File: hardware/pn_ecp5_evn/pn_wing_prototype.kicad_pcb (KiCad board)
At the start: 4 copper layers, 129.5 x 52.2 mm, 257 parts, among them J101 Screw_Terminal_01x02, J102 Conn_Coaxial, J103 Conn_02x20_Odd_Even, J104 Conn_Coaxial, J105 Conn_Coaxial, J106 Conn_Coaxial, J107 Conn_01x10, J201 Conn_Coaxial, J301 Conn_Coaxial, J401 Conn_Coaxial, J601 Conn_Coaxial, J701 Conn_Coaxial, J702 Conn_Coaxial, J703 Conn_Coaxial, U201 VEMI65AB-HCI, U202 LMX2594, U301 PAT1220-C-3DB, U302 TRF37A73, U303 PAT1220-C-3DB, U401 PAT1220-C-3DB, U402 TRF37A73, U403 PAT1220-C-3DB, U501 LM27761, U502 ADM7171ACPZ-3.3-R7, U503 TPS72301DB, U601 LM2904, U602 OPA2211, U701 SYM-63LH+, U702 ADG621, U703 OPA2211, U801 THS4551, U802 LT6657BHMS8-2.5, U901 ADS7868, U902 ADS7868, U903 Si8640BB-B-IU, U904 Si8640BB-B-IU, U905 Si8642BB-B-IU, X601 ABLNO

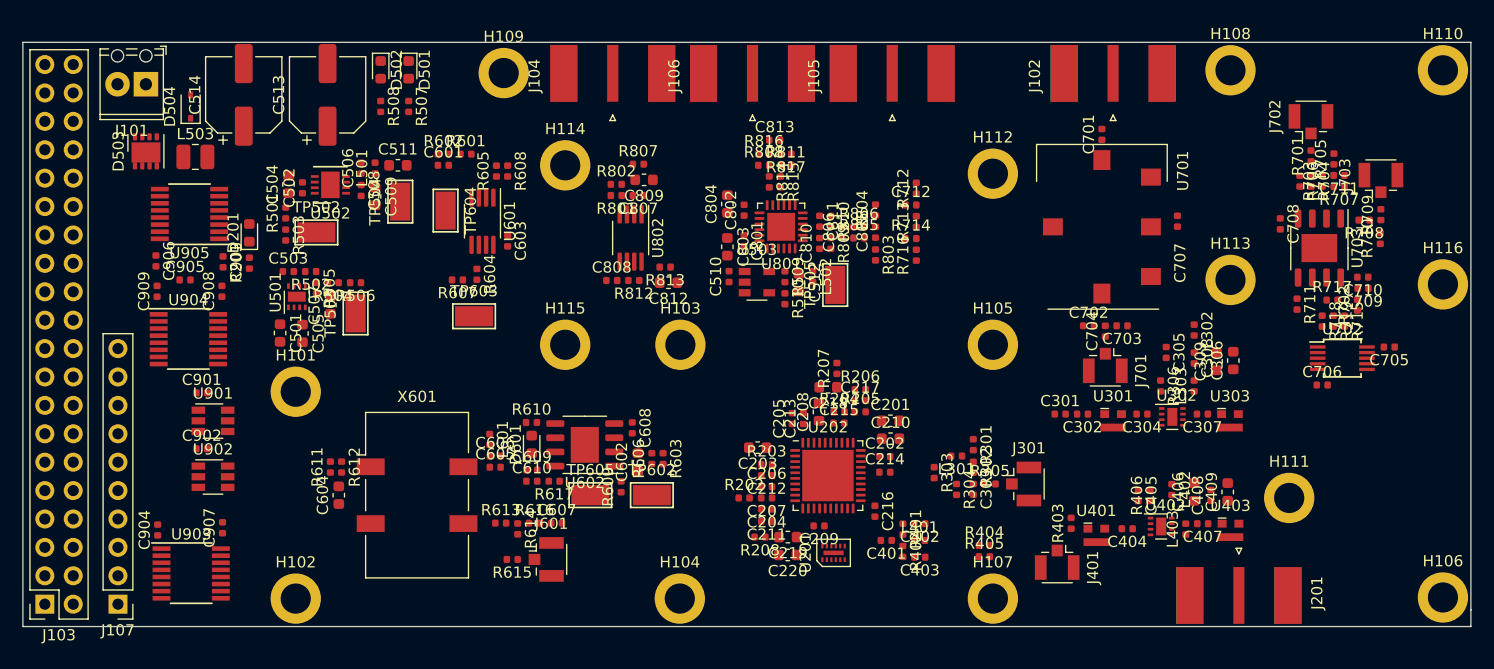
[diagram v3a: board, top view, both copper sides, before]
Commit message: work on routing phase noise downconverter
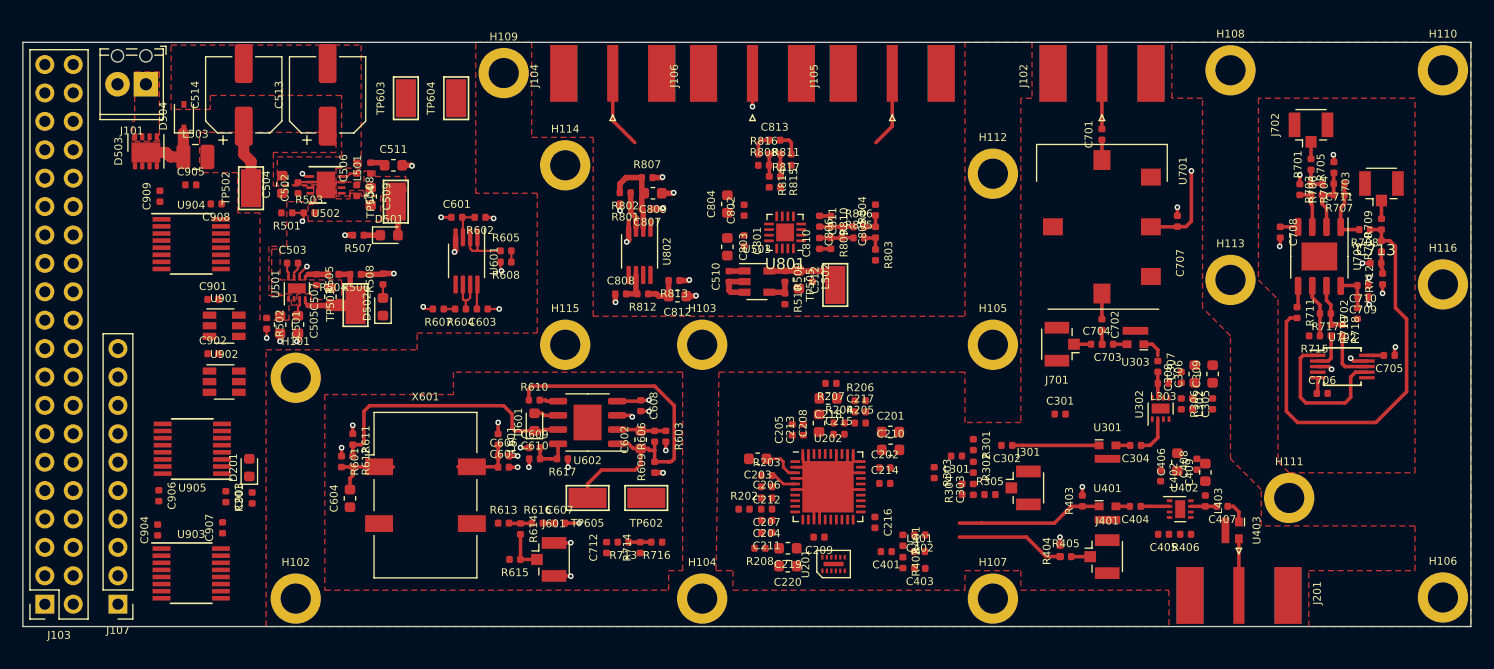
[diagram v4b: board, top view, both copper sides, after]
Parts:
- added C713: DNI, Capacitor_SMD:C_0402_1005Metric, F.Cu at (151.0, 85.5)
- U801: footprint Package_CSP:LFCSP-24-1EP_4x4mm_P0.5mm_EP2.5x2.5mm -> Package_DFN_QFN:VQFN-16-1EP_3x3mm_P0.5mm_EP1.6x1.6mm
- moved R712 42.5 mm to (151.6, 86.9)
- moved C712 41.0 mm to (82.2, 110.9), turned to 90 degrees
- moved R713 38.8 mm to (83.7, 110.5), turned to 180 degrees
- moved R714 36.7 mm to (85.2, 110.9), turned to 90 degrees
- moved R716 34.6 mm to (86.7, 110.5), turned to 180 degrees
- moved R601 29.7 mm to (58.5, 103.2), turned to 270 degrees
- moved D502 21.2 mm to (62.2, 89.4), turned to 90 degrees
- moved C903 21.0 mm to (48.1, 106.4)
- moved C906 21.0 mm to (42.1, 106.3)
- moved R201 21.0 mm to (50.5, 106.5)
- moved U905 21.0 mm to (45.1, 102.1)
- moved D201 21.0 mm to (50.2, 103.8)
- moved TP603 20.4 mm to (64.2, 70.8), turned to 90 degrees
- moved R508 15.4 mm to (62.2, 86.9), turned to 90 degrees
- moved D501 14.9 mm to (62.8, 83.0), turned to 0 degrees
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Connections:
- J103 pad 31: /isolator/BUF_~PD~_ISO -> /isolator/BUF_~PD
- U903 pad 13: /IF_G2 -> /LMX_CSB
- U903 pad 14: /IF_G1 -> /LMX_SDI
- U903 pad 3: /isolator/IF_G1 -> /isolator/LMX_SDI
- U903 pad 4: /isolator/IF_G2 -> /isolator/LMX_CS
- U904 pad 13: /LMX_SDI -> /IF_G2
- U904 pad 14: /LMX_CSB -> /IF_G1
- U904 pad 3: /isolator/LMX_CS -> /isolator/IF_G1
- U904 pad 4: /isolator/LMX_SDI -> /isolator/IF_G2
- U905 pad 11: /BUF_~PD -> /isolator/BUF_~PD
- U905 pad 6: /isolator/BUF_~PD~_ISO -> /BUF_~PD
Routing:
- net GND: track 0.00 -> 76.4 mm, vias 0 -> 37
- net Net-(R708-Pad1): track 0.00 -> 38.3 mm
- net Net-(C602-Pad1): track 0.00 -> 35.2 mm
- net Net-(D601-Pad1): track 0.00 -> 24.1 mm
- net Net-(R715-Pad1): track 0.00 -> 18.3 mm
- net Net-(C402-Pad1): track 0.00 -> 13.1 mm
- net -3V3: track 0.00 -> 12.8 mm, vias 0 -> 2
- net Net-(C707-Pad2): track 0.00 -> 10.6 mm, vias 0 -> 1
- net Net-(C403-Pad1): track 0.00 -> 9.72 mm
- net /adc/VOUT_P: track 0.00 -> 9.10 mm
- net Net-(C507-Pad1): track 0.00 -> 8.94 mm
- net /adc/VOUT_N: track 0.00 -> 8.92 mm
- net Net-(C302-Pad1): track 0.00 -> 7.77 mm
- net Net-(C807-Pad2): track 0.00 -> 7.70 mm
- net VPP: track 0.00 -> 6.82 mm
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- added copper zone on F.Cu, net +3V3
- added copper zone on F.Cu, net /power/VIN
- added copper zone on F.Cu, net GND
- added copper zone on F.Cu, net VPP
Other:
- net class microstrip added: clearance 0.15, trace_width 0.32, via_dia 0.5, via_drill 0.254
- rule via_min_size: 0.45 -> 0.5

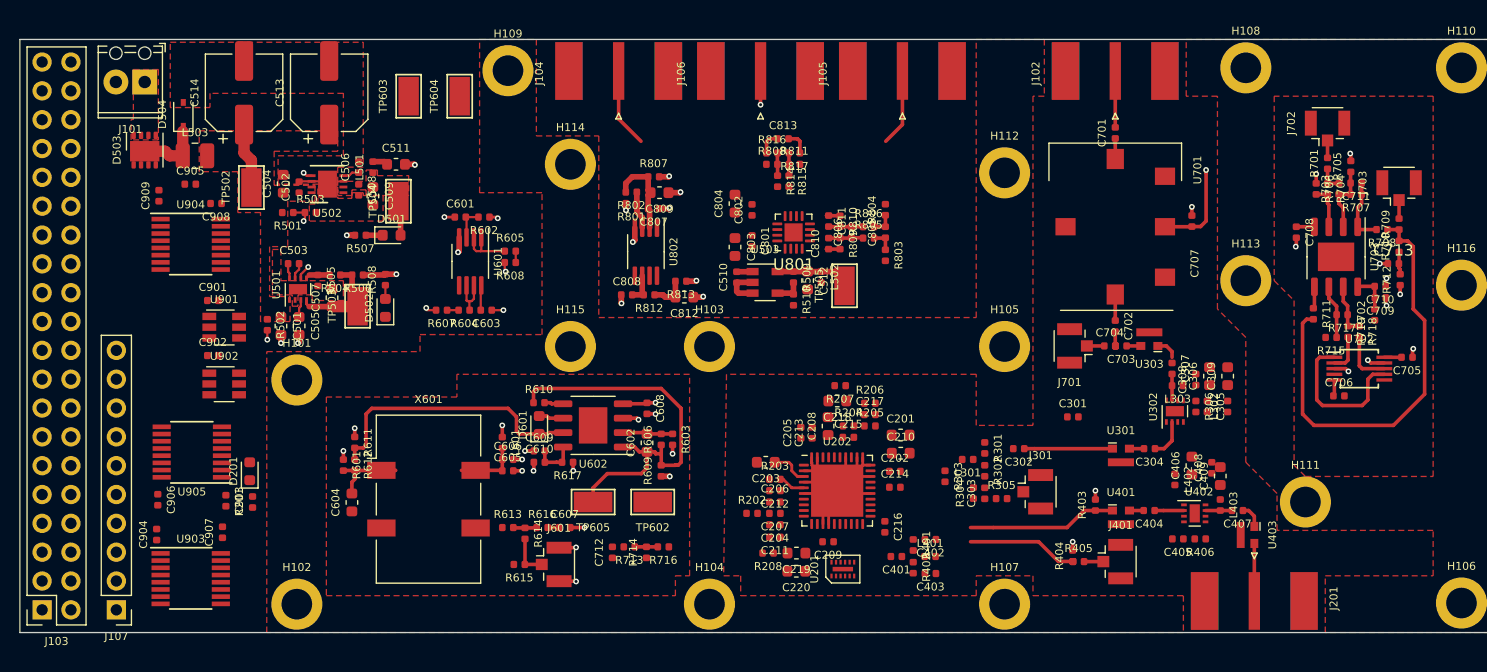
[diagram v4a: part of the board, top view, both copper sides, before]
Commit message: layout of phase noise downconverter
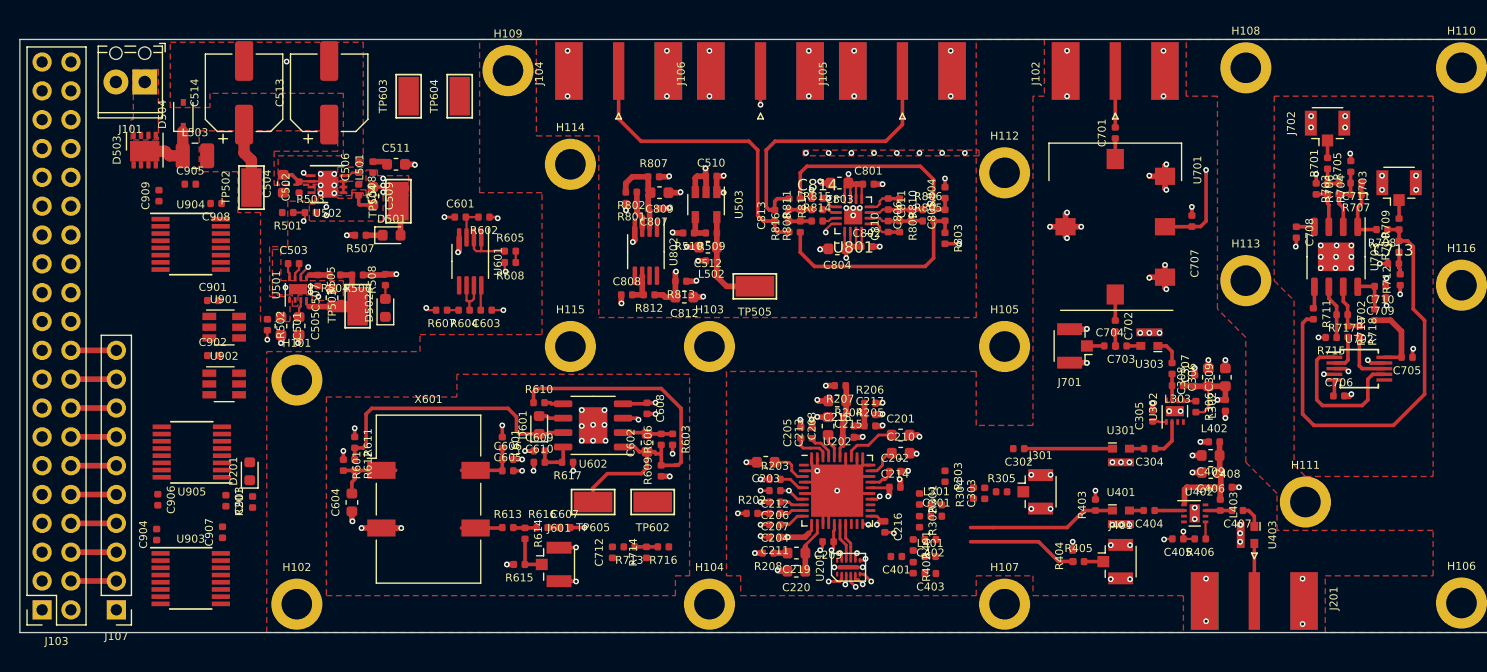
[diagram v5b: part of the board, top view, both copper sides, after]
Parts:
- added C814: 100 nF, Capacitor_SMD:C_0402_1005Metric, F.Cu at (100.2, 79.8)
- moved C301 14.9 mm to (110.7, 107.8)
- moved C801 11.4 mm to (104.8, 78.5), turned to 0 degrees
- moved R510 11.0 mm to (88.9, 82.8), turned to 180 degrees
- moved C803 10.8 mm to (102.2, 78.4), turned to 180 degrees
- moved C802 10.6 mm to (104.6, 84.0), turned to 0 degrees
- moved C804 9.86 mm to (102.0, 84.2), turned to 180 degrees
- moved L502 9.79 mm to (90.9, 85.2), turned to 180 degrees
- moved C512 9.27 mm to (90.6, 84.0), turned to 180 degrees
- moved C510 9.18 mm to (90.9, 77.8), turned to 0 degrees
- moved U503 8.60 mm to (90.5, 80.3), turned to 270 degrees
- moved R509 8.21 mm to (90.9, 82.8), turned to 180 degrees
- moved TP505 7.90 mm to (94.8, 87.5), turned to 180 degrees
- moved R301 7.30 mm to (109.2, 106.2)
- moved R302 7.29 mm to (109.2, 108.2)
- moved C813 6.80 mm to (96.5, 81.3), turned to 90 degrees
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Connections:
- J103 pad 1: /isolator/IF_G1 -> Net-(J103-Pad1)
- J103 pad 3: /isolator/IF_G2 -> Net-(J103-Pad3)
- J103 pad 35: Net-(J103-Pad35) -> /isolator/IF_G2
- J103 pad 37: Net-(J103-Pad37) -> /isolator/IF_G1
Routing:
- net GND: track 76.4 -> 135.7 mm, vias 37 -> 172
- net +3V3: track 6.19 -> 36.0 mm, vias 1 -> 16
- net /adc/VOUT_P: track 9.10 -> 27.2 mm
- net Net-(C805-Pad1): track 2.07 -> 19.7 mm
- net Net-(C805-Pad2): track 2.02 -> 19.4 mm
- net /adc/VOUT_N: track 8.92 -> 25.6 mm
- net Net-(C405-Pad1): track 0.00 -> 11.5 mm, vias 0 -> 1
- net Net-(C305-Pad1): track 0.00 -> 10.0 mm, vias 0 -> 1
- net -1V8: track 0.00 -> 8.77 mm, vias 0 -> 2
- net Net-(C215-Pad1): track 0.00 -> 6.56 mm
- net Net-(C219-Pad1): track 0.00 -> 5.38 mm, vias 0 -> 1
- net +3.3VA: track 4.65 -> 9.70 mm
- net Net-(C201-Pad1): track 0.00 -> 4.69 mm
- net Net-(J103-Pad8): track 0.00 -> 4.00 mm
- net Net-(J103-Pad6): track 0.00 -> 4.00 mm
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
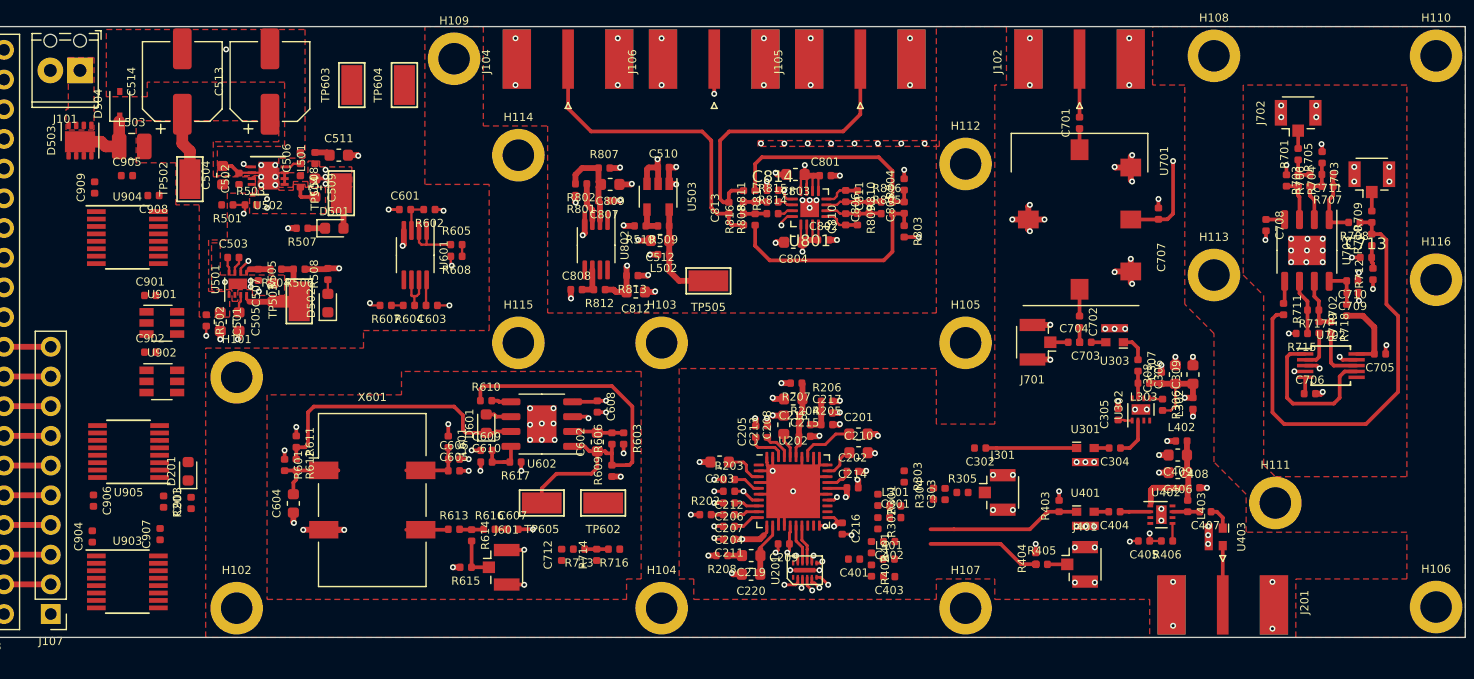
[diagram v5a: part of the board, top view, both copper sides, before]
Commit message: layout of phase noise downconverter
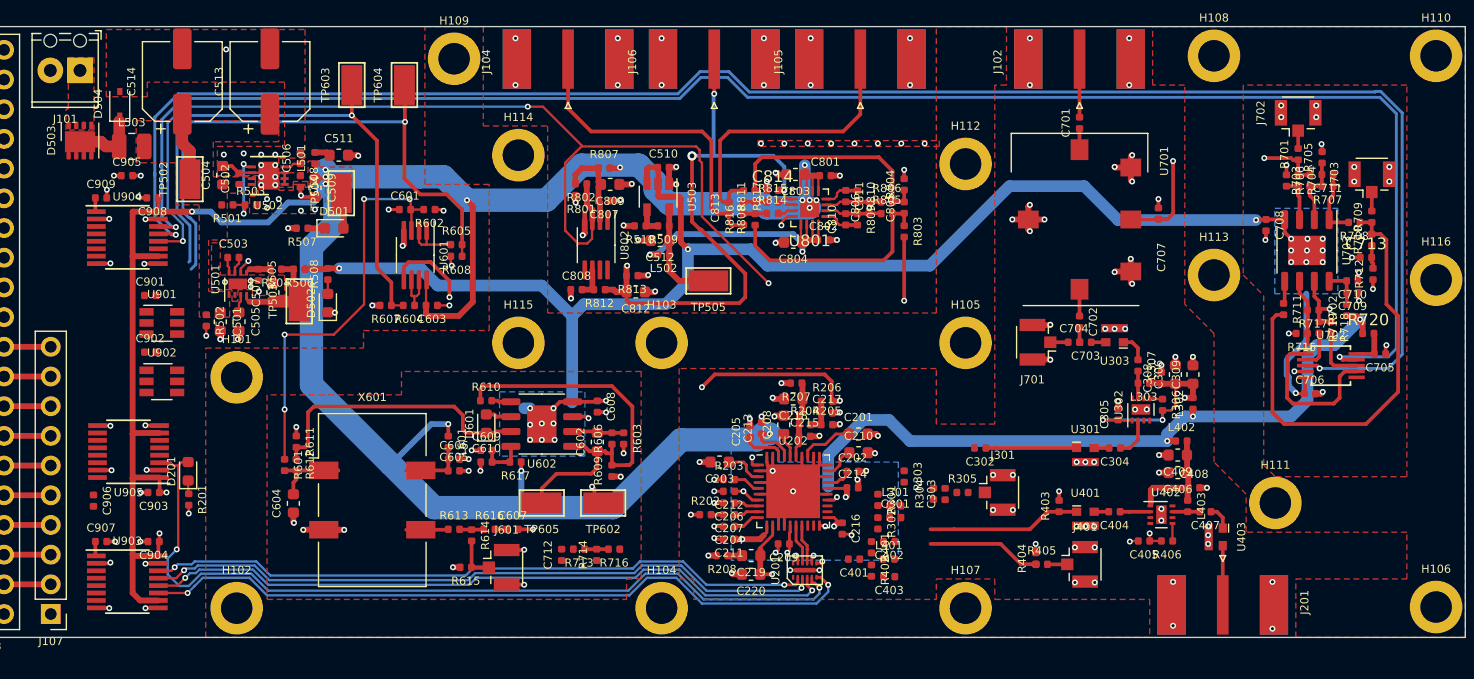
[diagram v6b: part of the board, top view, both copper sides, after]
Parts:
- added R720: R_Small, Resistor_SMD:R_0402_1005Metric, F.Cu at (151.2, 92.0)
- moved C904 5.27 mm to (47.3, 109.8), turned to 180 degrees
- moved C907 5.09 mm to (42.8, 109.8), turned to 0 degrees
- moved C903 1.16 mm to (47.3, 105.6), turned to 180 degrees
- moved C909 1.04 mm to (42.8, 80.4), turned to 0 degrees
- moved C213 0.58 mm to (99.3, 100.1)
- moved C205 0.50 mm to (98.3, 100.4)
- moved R201 0.36 mm to (50.3, 106.2), turned to 270 degrees
- moved C908 0.22 mm to (47.2, 80.4)
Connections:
- C705 pad 2: +3.3VA -> Net-(C705-Pad2)
- L601 pad 1: +3.3VA -> +3V3
- R617 pad 1: +3.3VA -> +3V3
- R702 pad 1: +3.3VA -> +3V3
- U702 pad 10: +3.3VA -> Net-(C705-Pad2)
- U903 pad 11: /LMX_SCK -> /LMX_CSB
- U903 pad 12: /LMX_CE -> /LMX_SDI
- U903 pad 13: /LMX_CSB -> /LMX_SCK
- U903 pad 14: /LMX_SDI -> /LMX_CE
- U903 pad 3: /isolator/LMX_SDI -> /isolator/LMX_CE
- U903 pad 4: /isolator/LMX_CS -> /isolator/LMX_SCK
- U903 pad 5: /isolator/LMX_CE -> /isolator/LMX_SDI
- U903 pad 6: /isolator/LMX_SCK -> /isolator/LMX_CS
- U904 pad 12: /isolator/SYNTH_VT_CS_ISO -> /BUF_~PD
- U904 pad 5: /isolator/SYNTH_VT_CS -> /isolator/BUF_~PD
- U905 pad 11: /isolator/BUF_~PD -> /isolator/SYNTH_VT_CS
- U905 pad 6: /BUF_~PD -> /isolator/SYNTH_VT_CS_ISO
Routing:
- net +3V3: track 36.0 -> 305.8 mm, vias 16 -> 24
- net /IF_G2: track 1.34 -> 152.1 mm, vias 1 -> 2
- net /IF_G1: track 1.55 -> 146.8 mm, vias 1 -> 2
- net -3V3: track 13.5 -> 132.1 mm, vias 20 -> 22
- net /BUF_~PD: track 4.81 -> 97.2 mm, vias 1 -> 4
- net Net-(C712-Pad2): track 0.80 -> 76.1 mm
- net /LMX_MUXout: track 1.29 -> 73.1 mm, vias 1 -> 2
- net /LMX_CSB: track 1.27 -> 62.3 mm, vias 1 -> 2
- net /LMX_SDI: track 1.30 -> 60.2 mm, vias 1 -> 2
- net /LMX_SCK: track 0.94 -> 58.4 mm, vias 1 -> 2
- net /LMX_CE: track 1.91 -> 57.5 mm, vias 1 -> 2
- net /VT_REF_TLM: track 1.00 -> 49.9 mm, vias 0 -> 1
- net /VT_SYNTH_TLM: track 1.02 -> 48.7 mm, vias 0 -> 1
- net /ref_pll/VT_SYNTH_UNBUF: track 0.65 -> 46.2 mm, vias 1 -> 3
- net /adc/ADC_VIN: track 5.93 -> 47.8 mm, vias 1 -> 2
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- added copper zone on B.Cu, net +3V3
- added copper zone on B.Cu, net -3V3
